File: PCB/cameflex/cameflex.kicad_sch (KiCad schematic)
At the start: 11 parts, among them P1 USB_C_Plug_USB2.0, U1 ATtiny85-20P, U2 KA78M05_TO252

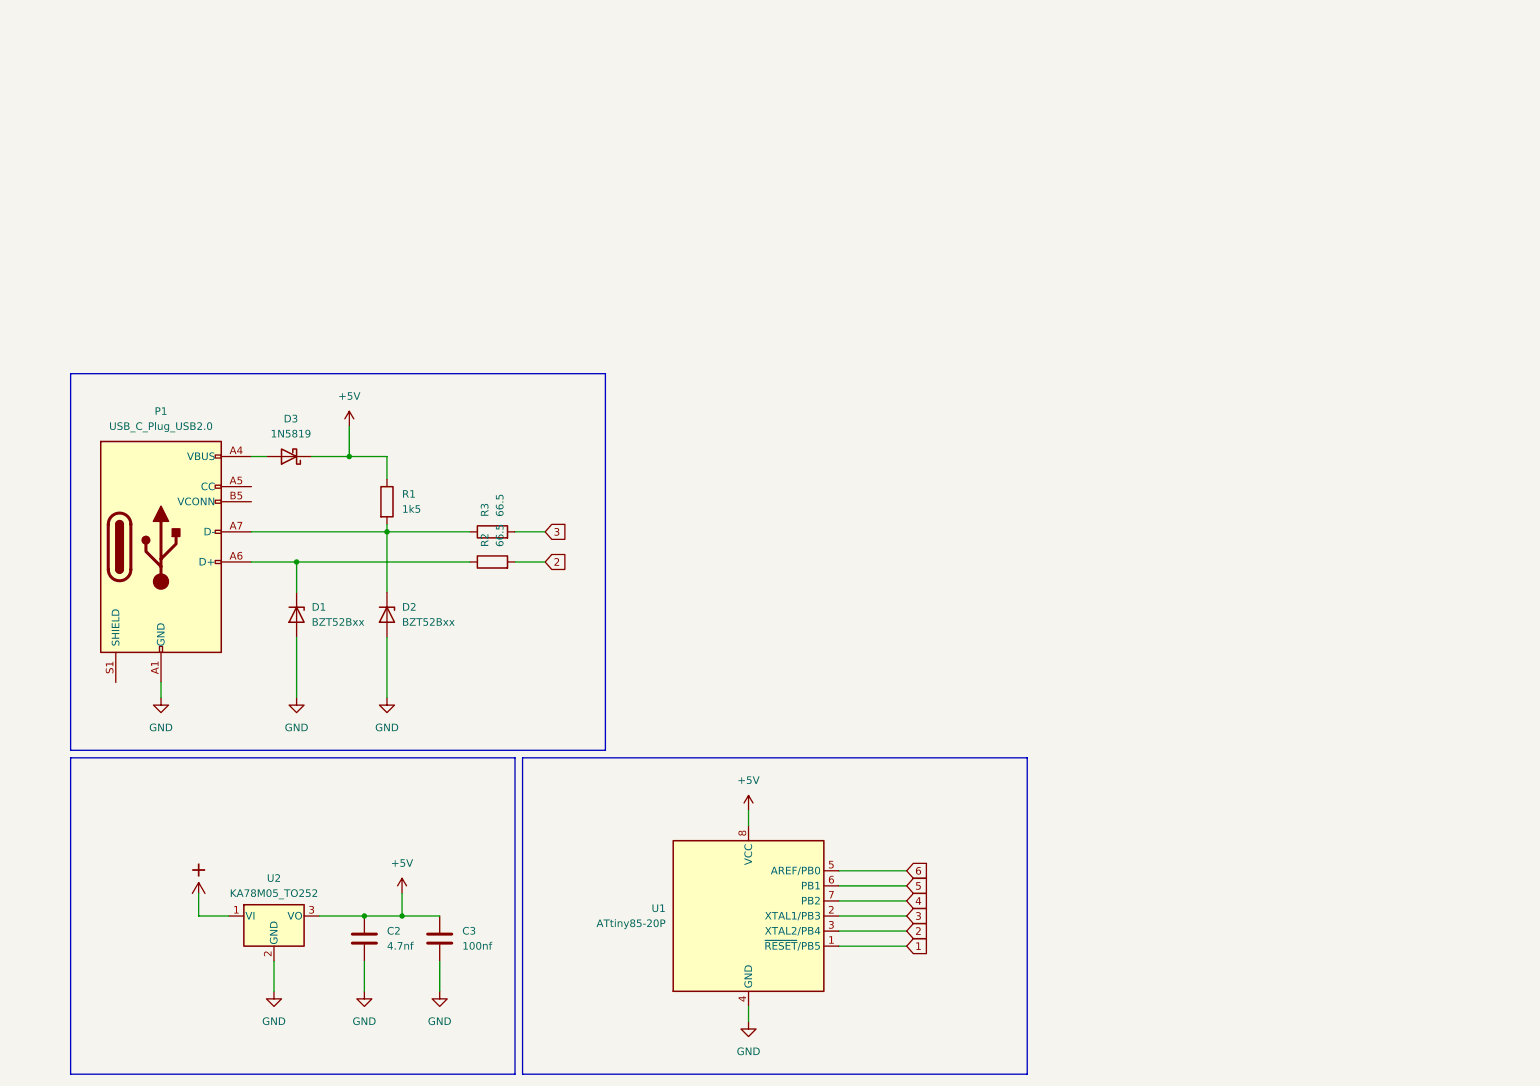
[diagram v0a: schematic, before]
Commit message: Update PCB design for Cameflex project
- Refactored the KiCad PCB file to include detailed layer definitions, general settings, and a new footprint for the Texas PicoStar DFN-3 component.
- Updated the schematic to replace the USB-C plug symbol with a polarized capacitor symbol, adjusting properties and pin configurations accordingly.
- Enhanced component descriptions and datasheet links for clarity and accuracy.
- Improved layout and organization of symbols and properties in the schematic for better readability.
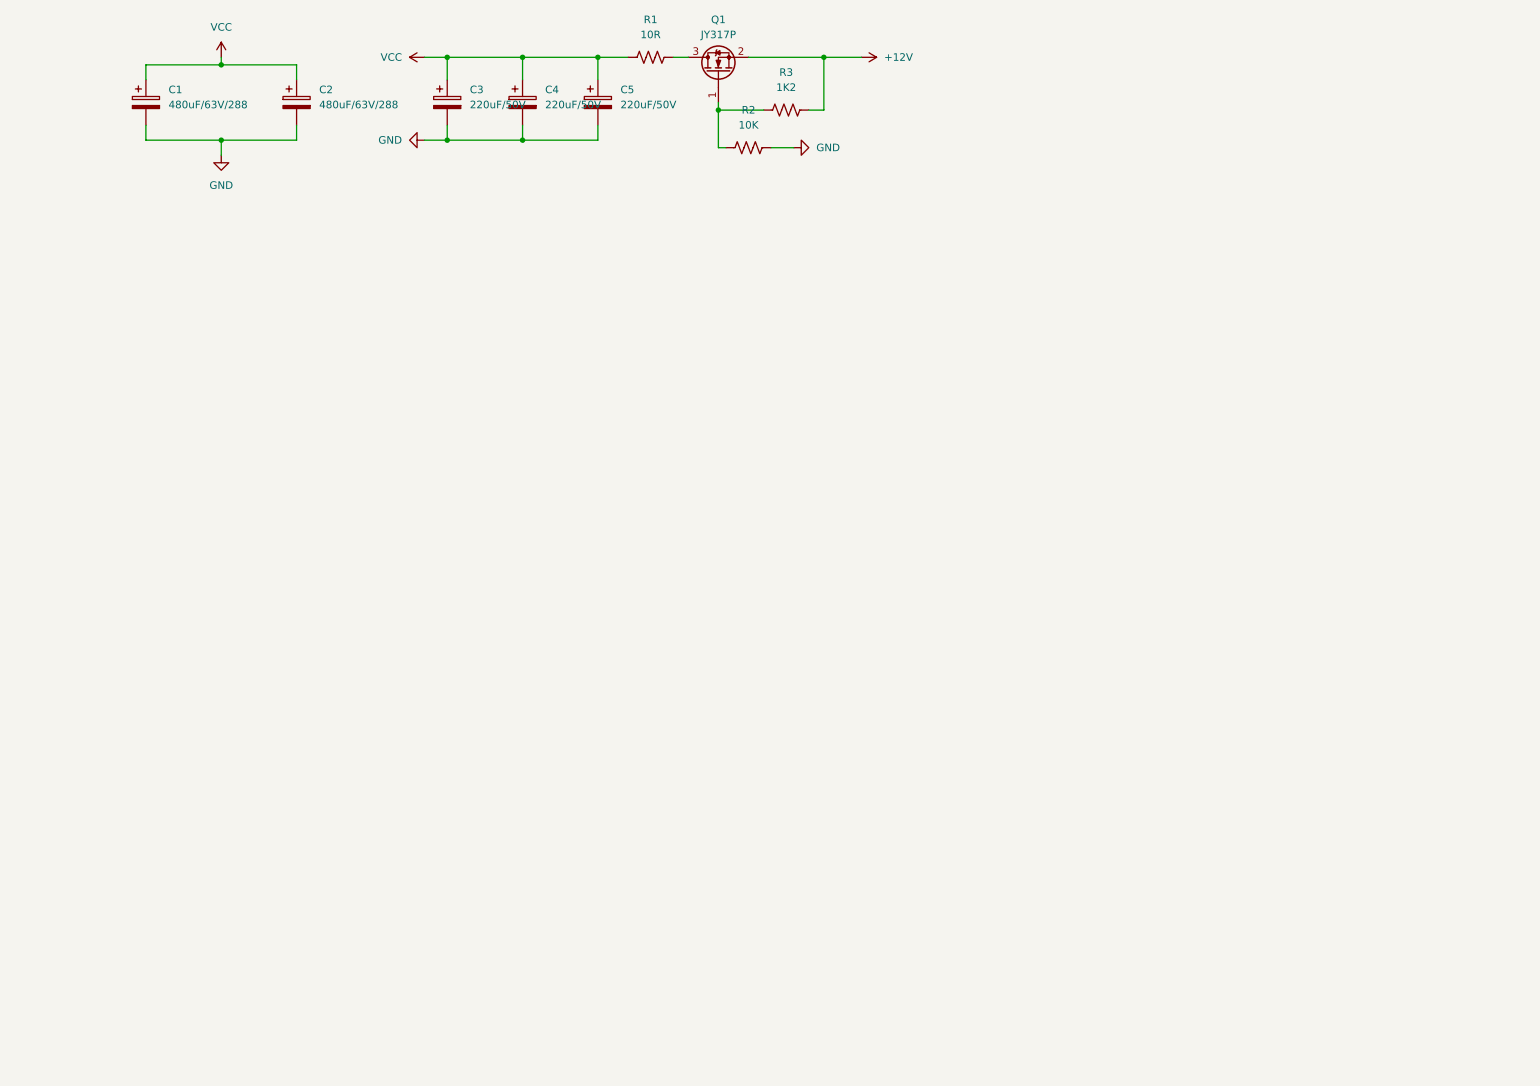
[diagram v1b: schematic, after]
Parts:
- removed C2: 4.7nf, symbol Device:C
- removed C3: 100nf, symbol Device:C
- removed D1, D2: BZT52Bxx, Diode_SMD:D_SOD-123F, symbol Diode:BZT52Bxx
- removed D3: 1N5819, Diode_THT:D_DO-41_SOD81_P10.16mm_Horizontal, symbol Diode:1N5819
- removed P1: USB_C_Plug_USB2.0, symbol Connector:USB_C_Plug_USB2.0
- removed R1: 1k5, symbol Device:R
- removed R2, R3: 66.5, symbol Device:R
- removed U1: ATtiny85-20P, Package_DIP:DIP-8_W7.62mm, symbol MCU_Microchip_ATtiny:ATtiny85-20P
- removed U2: KA78M05_TO252, Package_TO_SOT_SMD:TO-252-2, symbol Regulator_Linear:KA78M05_TO252
- added C1, C2: 480uF/63V/288, symbol Device:C_Polarized
- added C3, C4, C5: 220uF/50V, symbol Device:C_Polarized
- added Q1: JY317P, Package_DFN_QFN:Texas_PicoStar_DFN-3_0.69x0.60mm, symbol Transistor_FET:CSD13380F3
- added R1: 10R, symbol Device:R_US
- added R2: 10K, symbol Device:R_US
- added R3: 1K2, symbol Device:R_US
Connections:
- net GND: now also C1.2, C2.2, C3.2, C4.2, C5.2, R2.2
- new net: Q1.1 (G), R2.1, R3.1
- new net: Q1.3 (D), R1.2
- new net +12V: Q1.2 (S), R3.2
- new net VCC: C1.1, C2.1, C3.1, C4.1, C5.1, R1.1

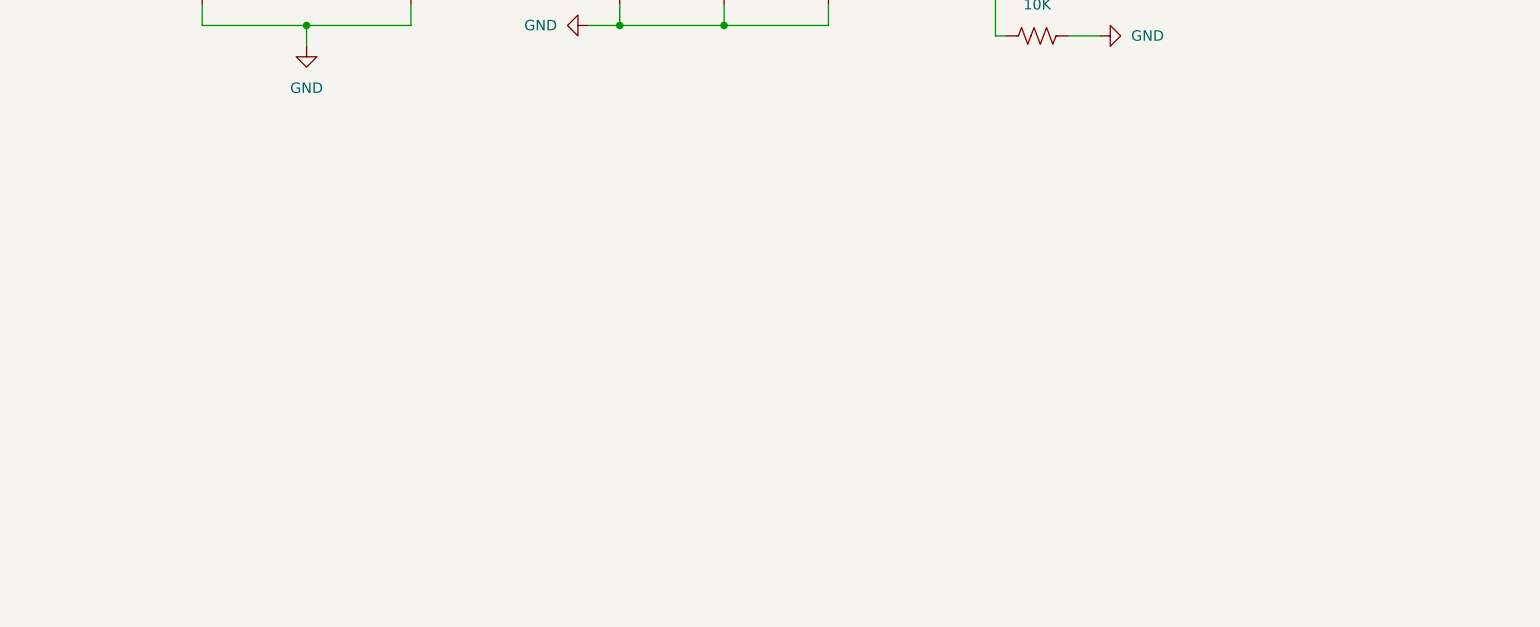
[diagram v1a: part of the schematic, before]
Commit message: Update Cameflex PCB files with new component definitions and error handling
- Added integration_disabled flag in the KiCad project file to manage integration settings.
- Introduced undefined_netclass error handling in the KiCad project configuration for improved design validation.
- Added a new generic connector symbol with detailed properties in the schematic, enhancing component representation and documentation.
- Removed outdated PDF documentation file to streamline project resources.
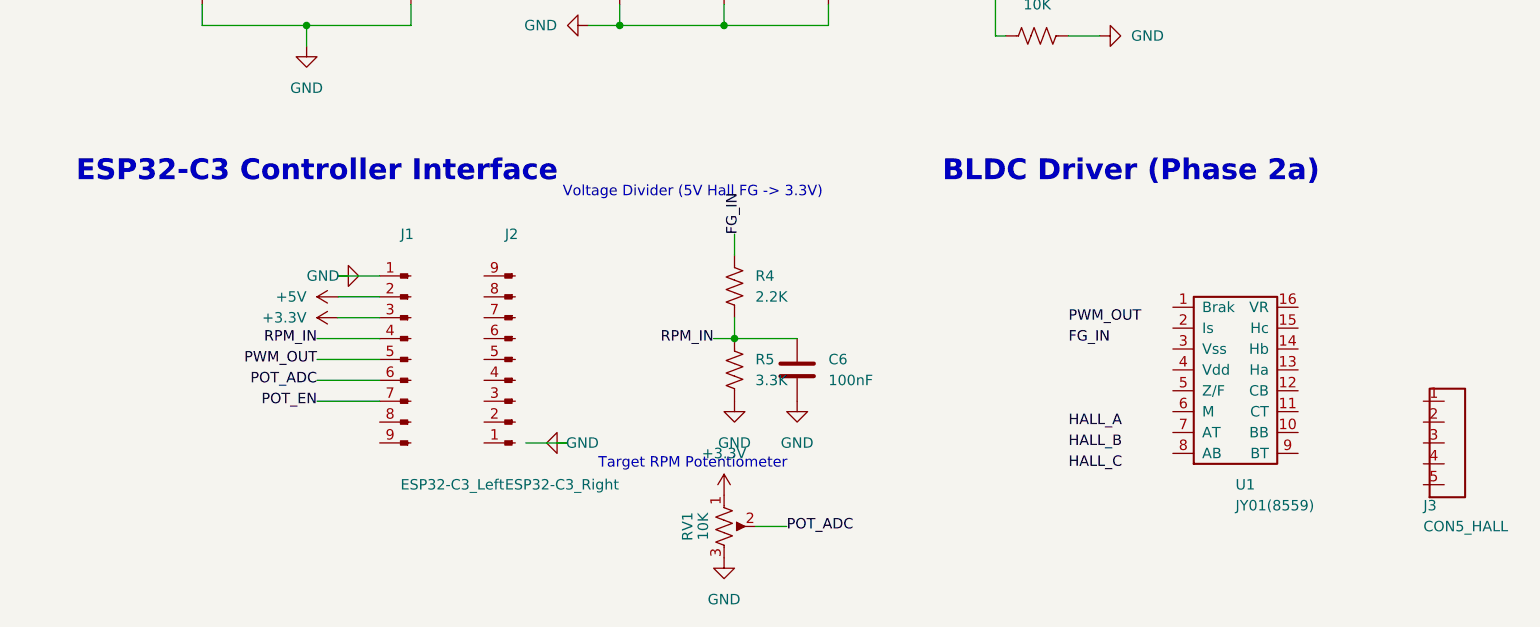
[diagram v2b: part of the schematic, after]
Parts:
- added C6: 100nF, Capacitor_SMD:C_0805_2012Metric, symbol Device:C
- added J1: ESP32-C3_Left, Connector_PinHeader_2.54mm:PinHeader_1x09_P2.54mm_Vertical, symbol Connector_Generic:Conn_01x09_Pin
- added J2: ESP32-C3_Right, Connector_PinHeader_2.54mm:PinHeader_1x09_P2.54mm_Vertical, symbol Connector_Generic:Conn_01x09_Pin
- added J3: CON5_HALL, Connector_PinHeader_2.54mm:PinHeader_1x05_P2.54mm_Vertical, symbol Connector_Generic:Conn_01x05_Pin
- added R4: 2.2K, Resistor_SMD:R_0805_2012Metric, symbol Device:R_US
- added R5: 3.3K, Resistor_SMD:R_0805_2012Metric, symbol Device:R_US
- added RV1: 10K, Potentiometer_THT:Potentiometer_Bourns_3296W_Vertical, symbol Device:R_Potentiometer_US
- added U1: JY01(8559), Package_SO:SOP-16_3.9x9.9mm_P1.27mm, symbol cameflex:JY01
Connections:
- net GND: now also C6.2, J1.1 (Pin_1), R5.2, RV1.3
- new net +3.3V: J1.3 (Pin_3), RV1.1
- new net +5V: J1.2 (Pin_2)
- new net FG_IN: R4.1
- new net POT_ADC: J1.6 (Pin_6), RV1.2
- new net POT_EN: J1.7 (Pin_7)
- new net PWM_OUT: J1.5 (Pin_5)
- new net RPM_IN: C6.1, J1.4 (Pin_4), R4.2, R5.1
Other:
- note added: "BLDC Driver (Phase 2a)"
- note added: "ESP32-C3 Controller Interface"
- note added: "Target RPM Potentiometer"
- note added: "Voltage Divider (5V Hall FG -> 3.3V)"

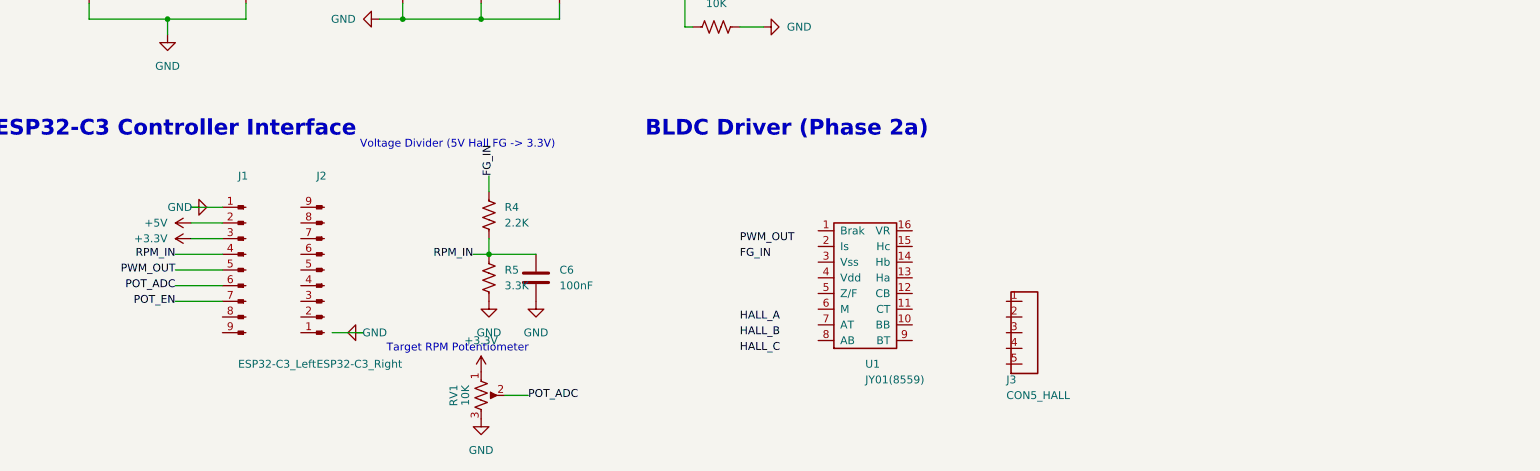
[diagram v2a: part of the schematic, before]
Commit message: Update Cameflex schematic to replace polarized capacitor with generic connectors
- Replaced the polarized capacitor symbol with a generic connector symbol for improved accuracy in the schematic.
- Updated properties, including reference and value, for the new connector symbols.
- Adjusted pin configurations and descriptions to reflect the new components.
- Enhanced organization and readability of the schematic by removing outdated properties and symbols.
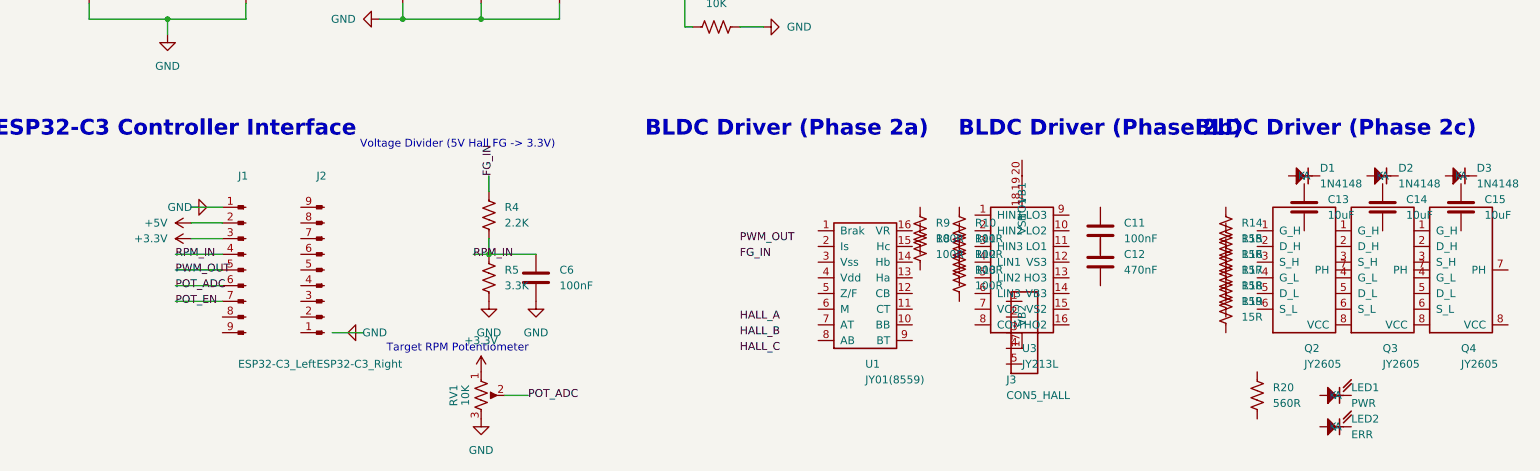
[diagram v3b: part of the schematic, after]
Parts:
- added C11: 100nF, Capacitor_SMD:C_0805_2012Metric, symbol Device:C
- added C12: 470nF, Capacitor_SMD:C_0805_2012Metric, symbol Device:C
- added C13, C14, C15: 10uF, Capacitor_SMD:C_0805_2012Metric, symbol Device:C
- added D1, D2, D3: 1N4148, Diode_SMD:D_SOD-123, symbol Device:D
- added LED1: PWR, LED_SMD:LED_0805_2012Metric, symbol Device:LED
- added LED2: ERR, LED_SMD:LED_0805_2012Metric, symbol Device:LED
- added Q2, Q3, Q4: JY2605, Package_DFN_QFN:DFN-8_5x6mm_P1.27mm, symbol cameflex:JY2605M_DualNMOS
- added R10, R11, R12, R13, R8, R9: 100R, Resistor_SMD:R_0805_2012Metric, symbol Device:R_US
- added R14, R15, R16, R17, R18, R19: 15R, Resistor_SMD:R_0805_2012Metric, symbol Device:R_US
- added R20: 560R, Resistor_SMD:R_0805_2012Metric, symbol Device:R_US
- added U3: JY213L, Package_SO:TSSOP-20_4.4x6.5mm_P0.65mm, symbol cameflex:JY213L
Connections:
- new net: R16.2, R19.1
- new net: R10.2, R13.1
- new net: R15.2, R18.1
- new net: R14.2, R17.1
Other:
- note added: "BLDC Driver (Phase 2b)"
- note added: "BLDC Driver (Phase 2c)"
